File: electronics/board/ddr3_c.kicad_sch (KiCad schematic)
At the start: 23 parts, among them U2 DDR3-78

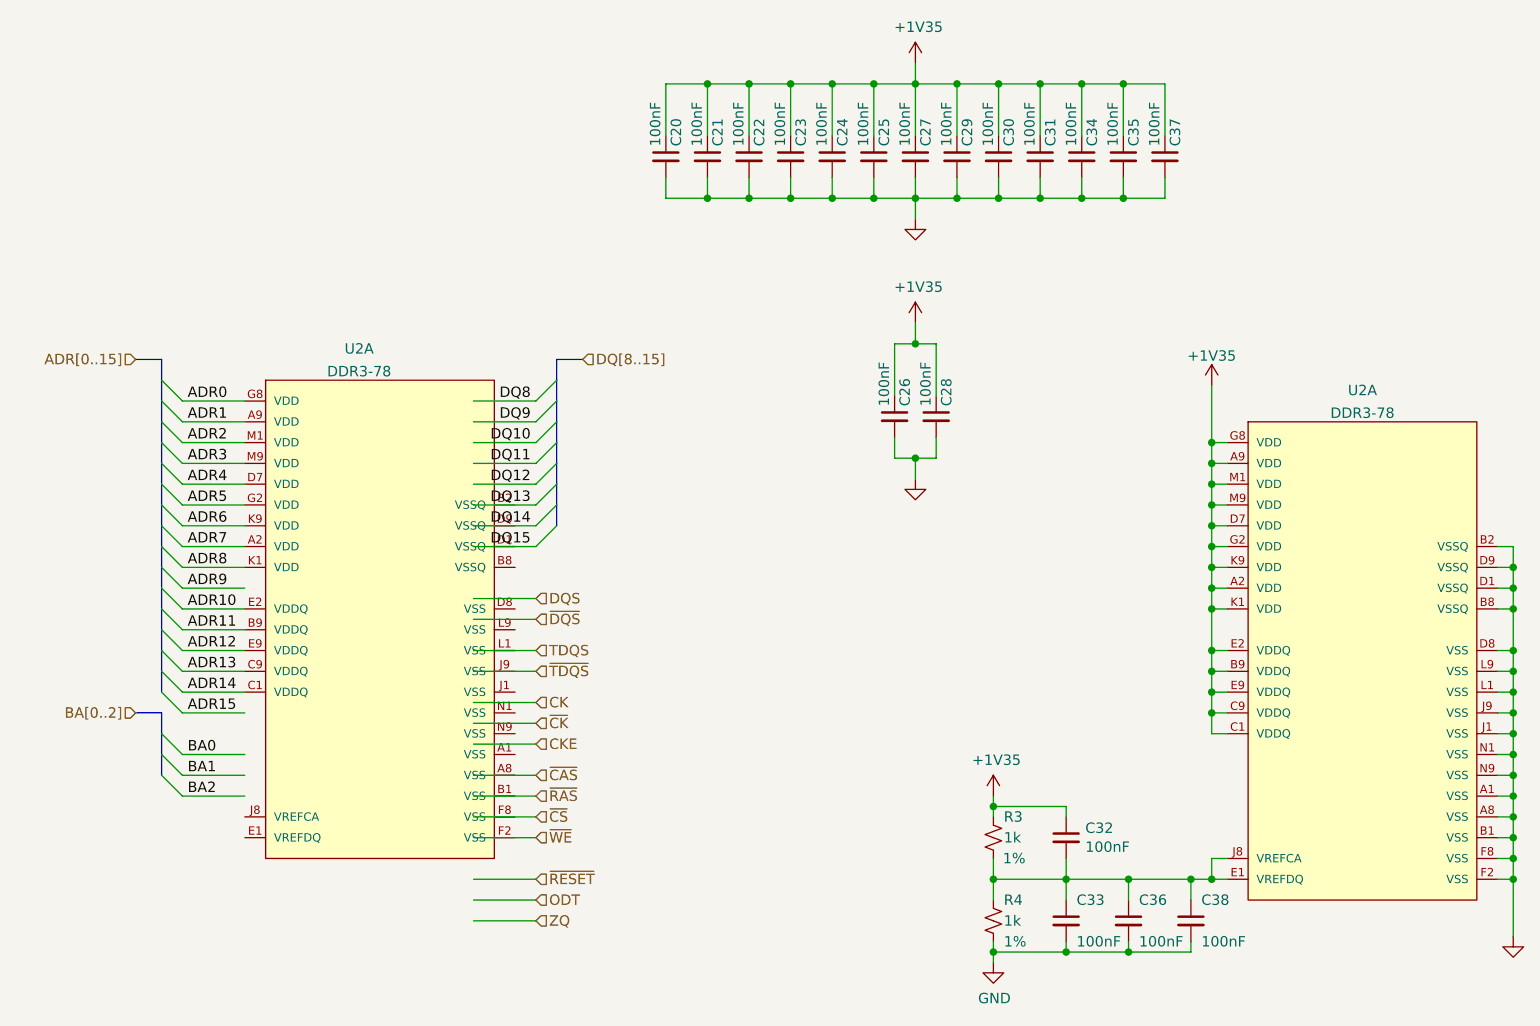
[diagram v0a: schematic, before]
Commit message: Added gitignore, fixed the part
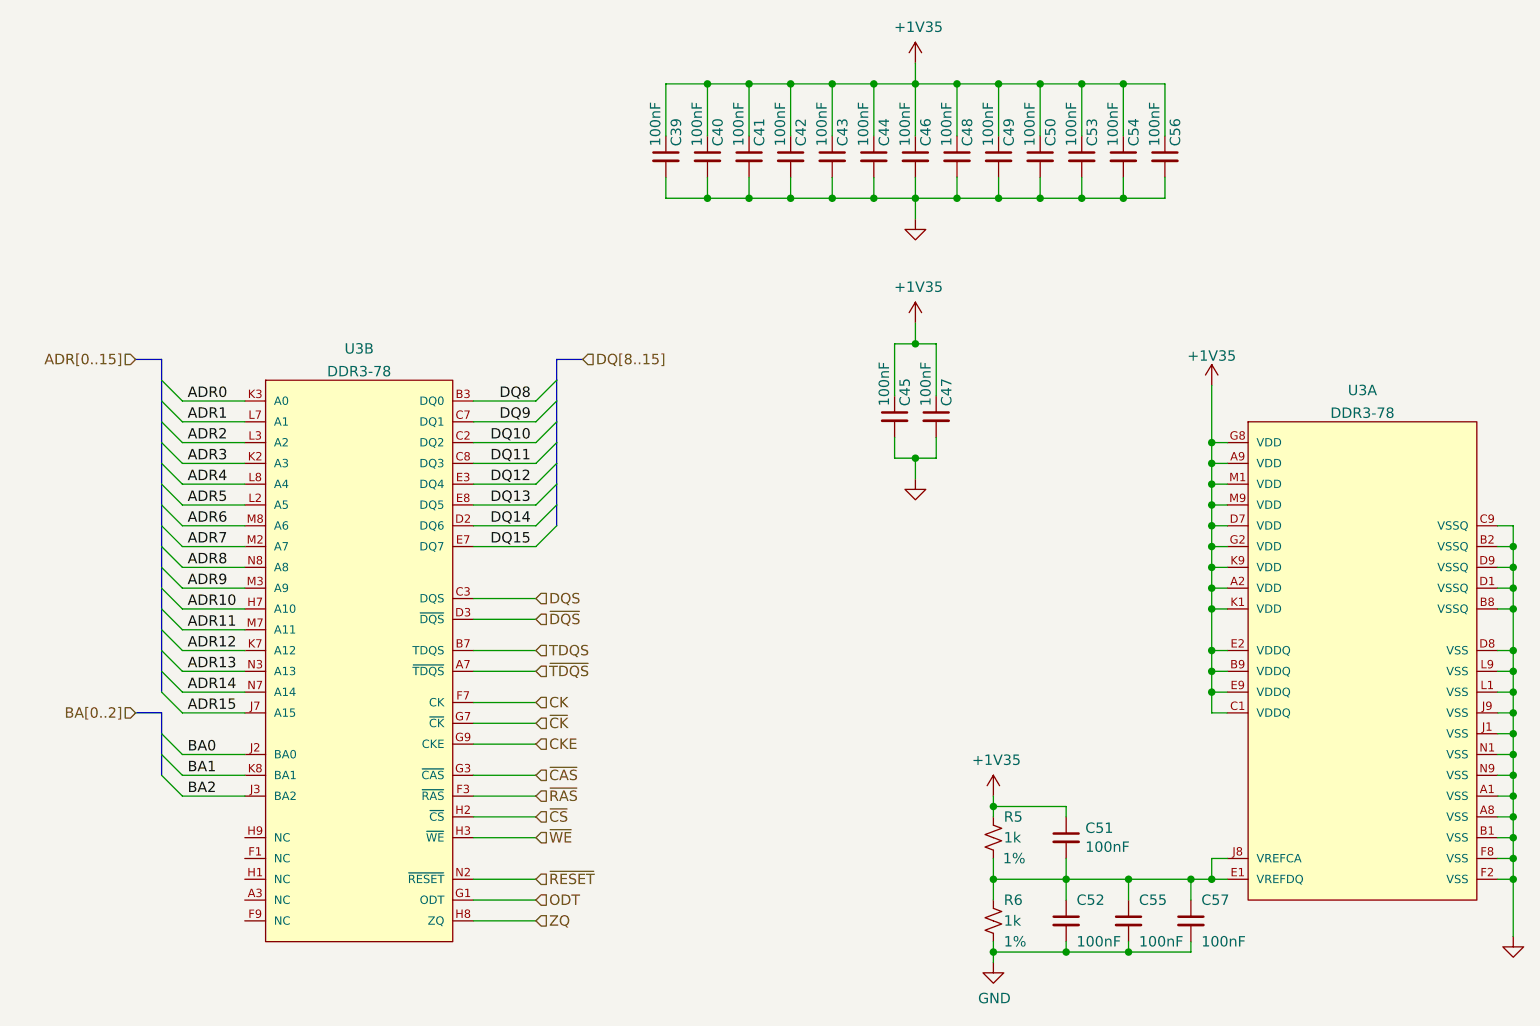
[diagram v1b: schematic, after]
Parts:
- renumbered C20 to C39, C21 to C40, C22 to C41, C23 to C42, C24 to C43, C25 to C44, C26 to C45, C27 to C46, C28 to C47, C29 to C48, C30 to C49, C31 to C50, C32 to C51, C33 to C52, C34 to C53, C35 to C54, C36 to C55, C37 to C56, C38 to C57, R3 to R5, R4 to R6, U2 to U3
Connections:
- net +1V35: no longer U3.C9 (VDDQ)
- net ADR0: now also U3.K3 (A0); no longer U3.G8 (VDD)
- net ADR1: now also U3.L7 (A1); no longer U3.A9 (VDD)
- net ADR10: now also U3.H7 (A10); no longer U3.E2 (VDDQ)
- net ADR11: now also U3.M7 (A11); no longer U3.B9 (VDDQ)
- net ADR12: now also U3.K7 (A12); no longer U3.E9 (VDDQ)
- net ADR13: now also U3.N3 (A13); no longer U3.C9 (VDDQ)
- net ADR14: now also U3.N7 (A14); no longer U3.C1 (VDDQ)
- net ADR15: now also U3.J7 (A15)
- net ADR2: now also U3.L3 (A2); no longer U3.M1 (VDD)
- net ADR3: now also U3.K2 (A3); no longer U3.M9 (VDD)
- net ADR4: now also U3.L8 (A4); no longer U3.D7 (VDD)
- net ADR5: now also U3.L2 (A5); no longer U3.G2 (VDD)
- net ADR6: now also U3.M8 (A6); no longer U3.K9 (VDD)
- net ADR7: now also U3.M2 (A7); no longer U3.A2 (VDD)
- net ADR8: now also U3.N8 (A8); no longer U3.K1 (VDD)
- net ADR9: now also U3.M3 (A9)
- net BA0: now also U3.J2 (BA0)
- net BA1: now also U3.K8 (BA1)
- net BA2: now also U3.J3 (BA2)
- net CK: now also U3.F7 (CK)
- net CKE: now also U3.G9 (CKE)
- net DQ10: now also U3.C2 (DQ2)
- net DQ11: now also U3.C8 (DQ3)
- net DQ12: now also U3.E3 (DQ4)
- net DQ13: now also U3.E8 (DQ5)
- net DQ14: now also U3.D2 (DQ6)
- net DQ15: now also U3.E7 (DQ7)
- net DQ8: now also U3.B3 (DQ0)
- net DQ9: now also U3.C7 (DQ1)
- net DQS: now also U3.C3 (DQS)
- net GND: now also U3.C9 (VSSQ)
- net ODT: now also U3.G1 (ODT)
- net TDQS: now also U3.B7 (TDQS)
- net ZQ: now also U3.H8 (ZQ)
- net ~{CAS}: now also U3.G3 (~{CAS})
- net ~{CK}: now also U3.G7 (~{CK})
- net ~{CS}: now also U3.H2 (~{CS})
- net ~{DQS}: now also U3.D3 (~{DQS})
- net ~{RAS}: now also U3.F3 (~{RAS})
- net ~{RESET}: now also U3.N2 (~{RESET})
- net ~{TDQS}: now also U3.A7 (~{TDQS})
- net ~{WE}: now also U3.H3 (~{WE})
